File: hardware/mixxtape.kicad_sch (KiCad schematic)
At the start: 69 parts, among them J1 USB-C-16P, J4 microSD (DNP), J5 PROG-JIG, SW1 REC, SW2 PLAY, SW3 TRACK, SW4 MODE, U1 ESP32-WROOM-32E-N4, U2 MSM261DHT006, U3 GD25Q128ESIG, U4 AMS1117-3.3, U8 SN74AHCT1G125

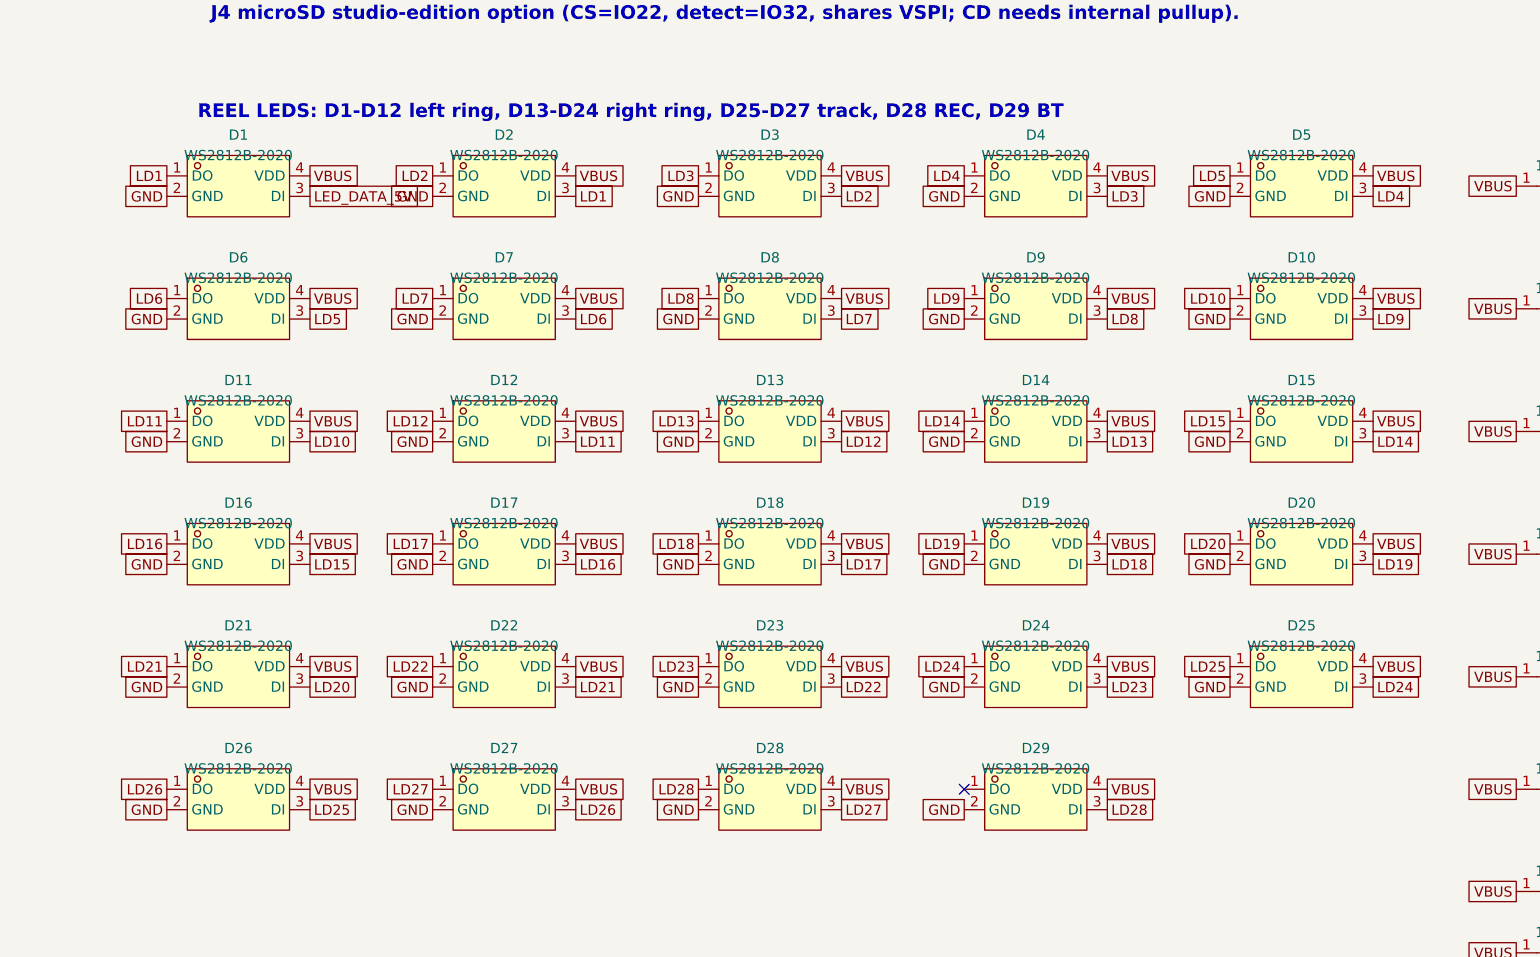
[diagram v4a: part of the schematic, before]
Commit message: hardware: fix a latent fatal LED footprint fault; clear 19 hidden DRC rules
The LED footprint was drawn for the GENUINE Worldsemi WS2812B-2020 (C965555)
and still carried that part number, while the BOM shipped the XINGLIGHT clone
C5349955, whose pad 1 is on the diagonally opposite corner. Every one of the
29 LEDs would have had VDD on the GND net and GND on VBUS - reverse-powered
across the 5 V rail, with no bodge possible on 0.225 mm of exposed copper.
ERC, DRC, the netlist and the BOM/CPL cross-check all passed, because every
one of them trusts the footprint.

Switched to XL-1615RGBC-2812B (C5349954), which Steven has used before: half
the price, double the stock, and its pin FUNCTIONS land in the same corners
the board already routes to, so the swap needed no re-routing - 0 unconnected.
Its pad NUMBERING is the manufacturer's (1=GND 2=DIN 3=VDD 4=DOUT), so the
symbol's pins were renumbered to match while leaving their positions and names
untouched, keeping every wire attached where it was.

J5, the only programming interface on the board, had F.Paste on all six bare
pogo pads - JLC would have stencilled solder onto them, leaving six uneven
blobs on the one path firmware can take onto a bare board. Removed, on the
board and in the library. Its silkscreen also read "BNT"; now "IO0".

Eleven DRC rules had been set to ignore or warning, hiding 144 findings.
Promoted 19 to error and fixed everything they surfaced: two dangling track
stubs, two missing courtyards, a starved thermal relief on D24, eight
hairline silk strokes at 0.06 mm that would not have printed, and text below
JLC's 1.0 mm / 0.15 mm floors. Added 7 GND stitching vias to the F.Cu ground
islands that hung off the plane by a single via, including U8's return path.
silk_edge_clearance stays a warning: the B-side art is a deliberate full
bleed and the fab clips it.

DRC 0 errors, 0 unconnected. ERC 0 errors, 0 warnings.
Board cost $8.62 -> $8.03.

Co-Authored-By: Claude Opus 5 <noreply@anthropic.com>
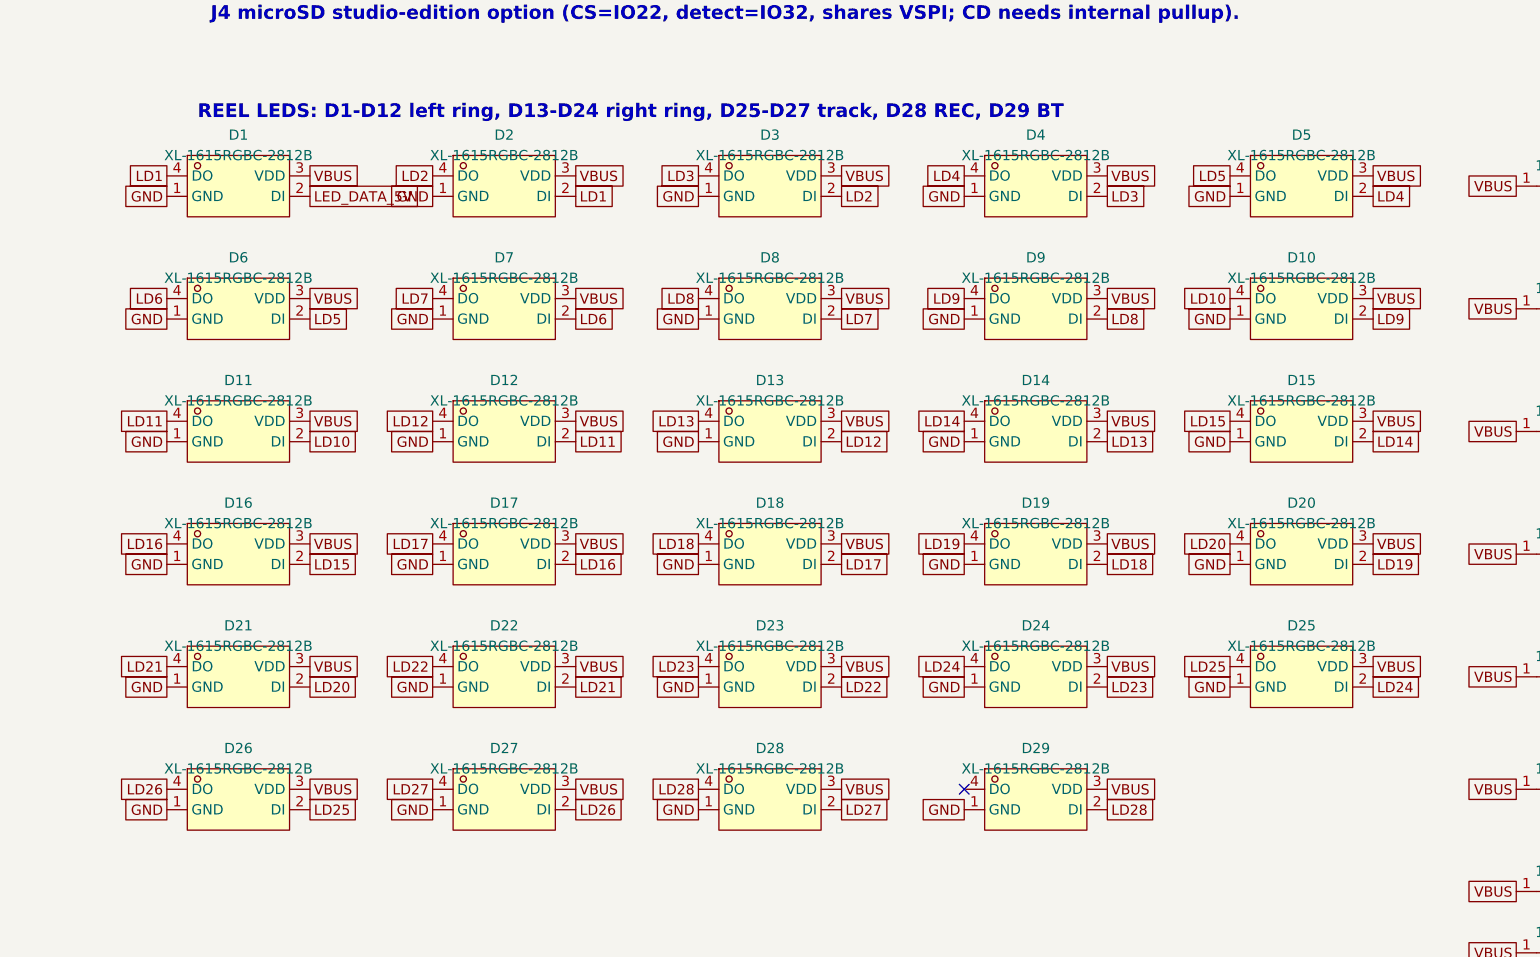
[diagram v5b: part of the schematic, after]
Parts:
- D1, D10, D11, D12, D13, D14, D15, D16, D17, D18, D19, D2, D20, D21, D22, D23, D24, D25, D26, D27, D28, D29, D3, D4, D5, D6, D7, D8, D9: value WS2812B-2020 -> XL-1615RGBC-2812B; footprint mixxtape_parts:LED-SMD_4P-L2.0-W2.0-TL_WS2812B-2020 -> mixxtape_parts:LED-SMD_4P-L1.6-W1.5_XL-1615RGBC-2812B; symbol mixxtape_parts:WS2812B-2020 -> mixxtape_parts:XL-1615RGBC-2812B; LCSC C5349955 -> C5349954
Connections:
- net GND: now also D1.1 (GND), D10.1 (GND), D11.1 (GND), D12.1 (GND), D13.1 (GND), D14.1 (GND), D15.1 (GND), D16.1 (GND), D17.1 (GND), D18.1 (GND), D19.1 (GND), D2.1 (GND), D20.1 (GND), D21.1 (GND), D22.1 (GND), D23.1 (GND), D24.1 (GND), D25.1 (GND), D26.1 (GND), D27.1 (GND), D28.1 (GND), D29.1 (GND), D3.1 (GND), D4.1 (GND), D5.1 (GND), D6.1 (GND), D7.1 (GND), D8.1 (GND), D9.1 (GND); no longer D1.2 (GND), D10.2 (GND), D11.2 (GND), D12.2 (GND), D13.2 (GND), D14.2 (GND), D15.2 (GND), D16.2 (GND), D17.2 (GND), D18.2 (GND), D19.2 (GND), D2.2 (GND), D20.2 (GND), D21.2 (GND), D22.2 (GND), D23.2 (GND), D24.2 (GND), D25.2 (GND), D26.2 (GND), D27.2 (GND), D28.2 (GND), D29.2 (GND), D3.2 (GND), D4.2 (GND), D5.2 (GND), D6.2 (GND), D7.2 (GND), D8.2 (GND), D9.2 (GND)
- net LD1: now also D1.4 (DO), D2.2 (DI); no longer D1.1 (DO), D2.3 (DI)
- net LD10: now also D10.4 (DO), D11.2 (DI); no longer D10.1 (DO), D11.3 (DI)
- net LD11: now also D11.4 (DO), D12.2 (DI); no longer D11.1 (DO), D12.3 (DI)
- net LD12: now also D12.4 (DO), D13.2 (DI); no longer D12.1 (DO), D13.3 (DI)
- net LD13: now also D13.4 (DO), D14.2 (DI); no longer D13.1 (DO), D14.3 (DI)
- net LD14: now also D14.4 (DO), D15.2 (DI); no longer D14.1 (DO), D15.3 (DI)
- net LD15: now also D15.4 (DO), D16.2 (DI); no longer D15.1 (DO), D16.3 (DI)
- net LD16: now also D16.4 (DO), D17.2 (DI); no longer D16.1 (DO), D17.3 (DI)
- net LD17: now also D17.4 (DO), D18.2 (DI); no longer D17.1 (DO), D18.3 (DI)
- net LD18: now also D18.4 (DO), D19.2 (DI); no longer D18.1 (DO), D19.3 (DI)
- net LD19: now also D19.4 (DO), D20.2 (DI); no longer D19.1 (DO), D20.3 (DI)
- net LD2: now also D2.4 (DO), D3.2 (DI); no longer D2.1 (DO), D3.3 (DI)
- net LD20: now also D20.4 (DO), D21.2 (DI); no longer D20.1 (DO), D21.3 (DI)
- net LD21: now also D21.4 (DO), D22.2 (DI); no longer D21.1 (DO), D22.3 (DI)
- net LD22: now also D22.4 (DO), D23.2 (DI); no longer D22.1 (DO), D23.3 (DI)
- net LD23: now also D23.4 (DO), D24.2 (DI); no longer D23.1 (DO), D24.3 (DI)
- net LD24: now also D24.4 (DO), D25.2 (DI); no longer D24.1 (DO), D25.3 (DI)
- net LD25: now also D25.4 (DO), D26.2 (DI); no longer D25.1 (DO), D26.3 (DI)
- net LD26: now also D26.4 (DO), D27.2 (DI); no longer D26.1 (DO), D27.3 (DI)
- net LD27: now also D27.4 (DO), D28.2 (DI); no longer D27.1 (DO), D28.3 (DI)
- net LD28: now also D28.4 (DO), D29.2 (DI); no longer D28.1 (DO), D29.3 (DI)
- net LD3: now also D3.4 (DO), D4.2 (DI); no longer D3.1 (DO), D4.3 (DI)
- net LD4: now also D4.4 (DO), D5.2 (DI); no longer D4.1 (DO), D5.3 (DI)
- net LD5: now also D5.4 (DO), D6.2 (DI); no longer D5.1 (DO), D6.3 (DI)
- net LD6: now also D6.4 (DO), D7.2 (DI); no longer D6.1 (DO), D7.3 (DI)
- net LD7: now also D7.4 (DO), D8.2 (DI); no longer D7.1 (DO), D8.3 (DI)
- net LD8: now also D8.4 (DO), D9.2 (DI); no longer D8.1 (DO), D9.3 (DI)
- net LD9: now also D10.2 (DI), D9.4 (DO); no longer D10.3 (DI), D9.1 (DO)
- net LED_DATA_5V: now also D1.2 (DI); no longer D1.3 (DI)
- net VBUS: now also D1.3 (VDD), D10.3 (VDD), D11.3 (VDD), D12.3 (VDD), D13.3 (VDD), D14.3 (VDD), D15.3 (VDD), D16.3 (VDD), D17.3 (VDD), D18.3 (VDD), D19.3 (VDD), D2.3 (VDD), D20.3 (VDD), D21.3 (VDD), D22.3 (VDD), D23.3 (VDD), D24.3 (VDD), D25.3 (VDD), D26.3 (VDD), D27.3 (VDD), D28.3 (VDD), D29.3 (VDD), D3.3 (VDD), D4.3 (VDD), D5.3 (VDD), D6.3 (VDD), D7.3 (VDD), D8.3 (VDD), D9.3 (VDD); no longer D1.4 (VDD), D10.4 (VDD), D11.4 (VDD), D12.4 (VDD), D13.4 (VDD), D14.4 (VDD), D15.4 (VDD), D16.4 (VDD), D17.4 (VDD), D18.4 (VDD), D19.4 (VDD), D2.4 (VDD), D20.4 (VDD), D21.4 (VDD), D22.4 (VDD), D23.4 (VDD), D24.4 (VDD), D25.4 (VDD), D26.4 (VDD), D27.4 (VDD), D28.4 (VDD), D29.4 (VDD), D3.4 (VDD), D4.4 (VDD), D5.4 (VDD), D6.4 (VDD), D7.4 (VDD), D8.4 (VDD), D9.4 (VDD)
